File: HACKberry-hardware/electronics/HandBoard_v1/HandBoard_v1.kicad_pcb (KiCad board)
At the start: 2 copper layers, 60.8 x 54.8 mm, 12 parts, among them CON1 BARREL_JACK_MJ179PH, SW1:MAX1 SW_PUSH_SKRGAQD010, SW2:MIN1 SW_PUSH_SKRGAQD010, SW3:Thumb1 SW_PUSH_SKRGAQD010, SW4:Middle1 SW_PUSH_SKRGAQD010, SW5 SWITCH_SS-12SDP2, U1 3-CONDUCTOR_MINIATUIRE_JACK_M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, U2 Arduino_Micro, U3 Seed_Studio_Adjustable_DC/DC_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, U4 Servo_Motor_S03N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

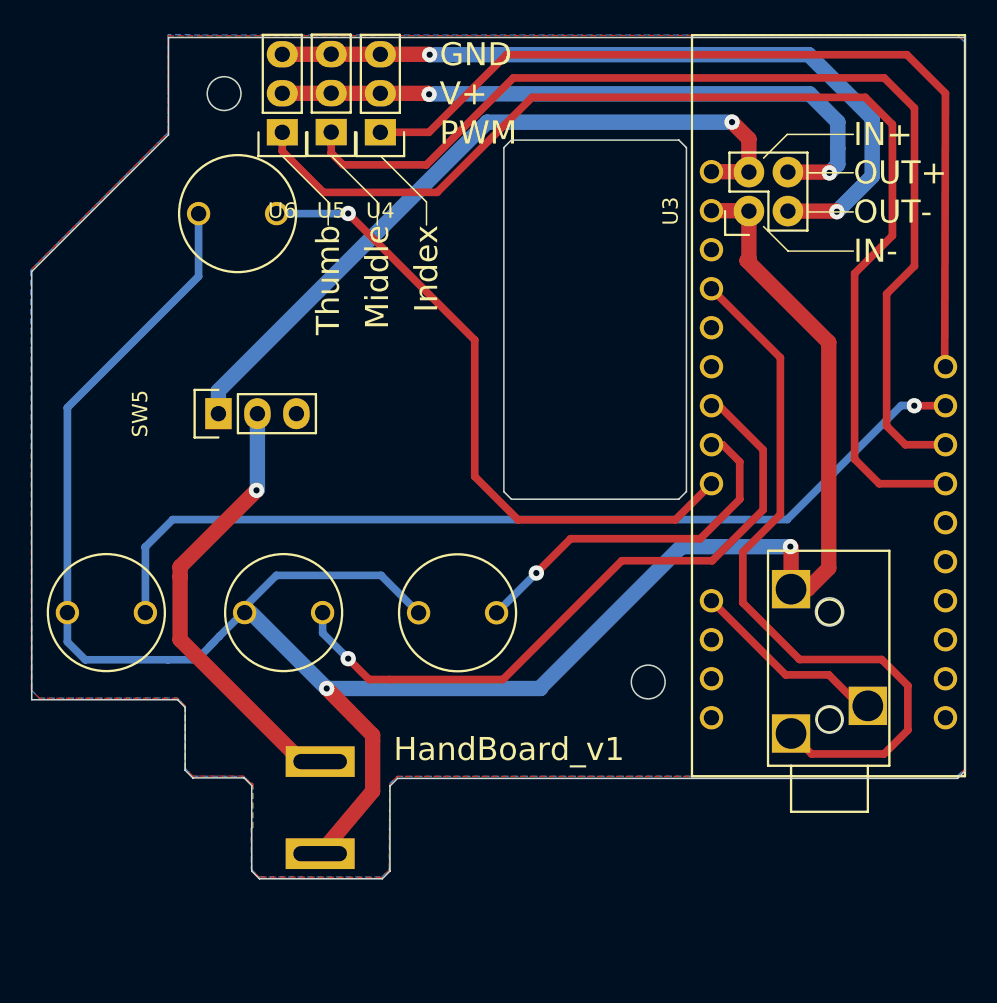
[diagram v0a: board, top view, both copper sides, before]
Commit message: add poly switch to protect servo motor
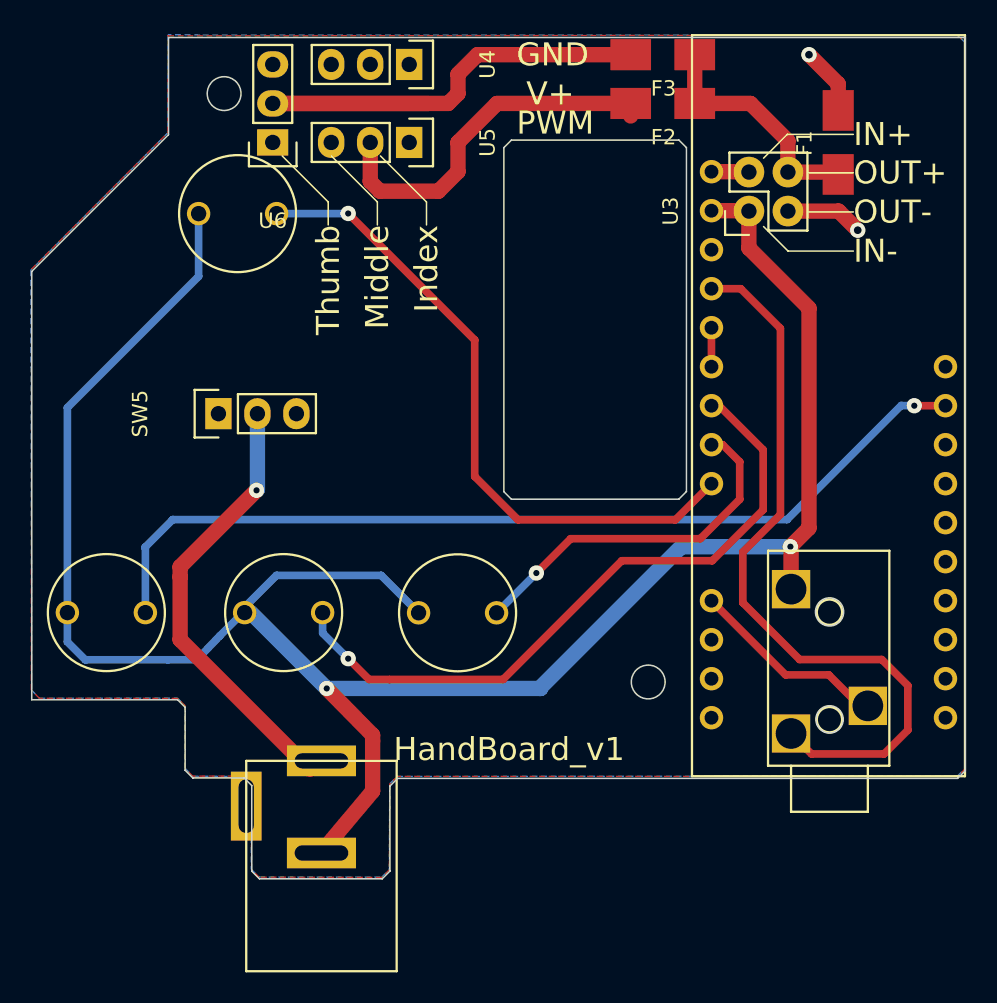
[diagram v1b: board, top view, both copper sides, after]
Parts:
- added F1: FUSE_Hackberry_large, Fuse_Holders_and_Fuses:Fuse_SMD1206_HandSoldering, F.Cu at (149.1, 87.9)
- added F2: FUSE_Hackberry, Fuse_Holders_and_Fuses:Fuse_SMD1206_HandSoldering, F.Cu at (137.7, 85.3)
- added F3: FUSE_Hackberry, Fuse_Holders_and_Fuses:Fuse_SMD1206_HandSoldering, F.Cu at (137.7, 82.1)
- CON1: value BARREL_JACK_MJ179PH -> BARREL_JACK
- U1: value 3-CONDUCTOR_MINIATUIRE_JACK_MJ-4535-3 -> 3-CONDUCTOR_MINIATUIRE_JACK_MJ-4535-3-RESCUE-HandBoard_v1
- U5, U6: value Servo_Motor_MG90S -> Servo_Motor_ES08MD
- moved U5 5.12 mm to (121.2, 87.9), turned to 270 degrees
- moved U4 4.80 mm to (121.2, 82.8), turned to 270 degrees
- moved U6 0.91 mm to (112.3, 87.9)
- moved CON1 0.10 mm to (115.5, 141.8)
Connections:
- SW1:MAX1 pad 1: Net-(CON1-Pad3) -> Net-(CON1-Pad2)
- SW2:MIN1 pad 1: Net-(CON1-Pad3) -> Net-(CON1-Pad2)
- SW3:Thumb1 pad 1: Net-(CON1-Pad3) -> Net-(CON1-Pad2)
- SW4:Middle1 pad 1: Net-(CON1-Pad3) -> Net-(CON1-Pad2)
- U1 pad 1: Net-(CON1-Pad3) -> Net-(CON1-Pad2)
- U2 pad 5V: Net-(U2-Pad5V) -> Net-(U1-Pad2)
- U2 pad GND: Net-(U2-PadGND) -> Net-(CON1-Pad2)
- U3 pad 2: Net-(CON1-Pad3) -> Net-(CON1-Pad2)
- U3 pad 4: Net-(U3-Pad4) -> Net-(F1-Pad1)
- U4 pad 2: Net-(U3-Pad4) -> Net-(F1-Pad2)
- U5 pad 2: Net-(U3-Pad4) -> Net-(F2-Pad2)
- U6 pad 2: Net-(U3-Pad4) -> Net-(F3-Pad2)
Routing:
- net Net-(CON1-Pad3): track 144.4 -> 0.00 mm, vias 2 -> 0
- net Net-(CON1-Pad2): track 0.00 -> 142.3 mm, vias 0 -> 2
- net Net-(U3-Pad4): track 43.2 -> 0.00 mm, vias 2 -> 0
- net Net-(F1-Pad2): track 0.00 -> 36.5 mm, vias 0 -> 1
- net Net-(F3-Pad2): track 0.00 -> 35.5 mm
- net Net-(F2-Pad2): track 0.00 -> 24.1 mm
- net Net-(F1-Pad1): track 0.00 -> 16.3 mm
- net Net-(U3-Pad3): track 50.4 -> 62.3 mm, vias 2 -> 1
- net Net-(U2-Pad5): track 68.6 -> 58.1 mm
- net Net-(U1-Pad2): track 41.7 -> 49.1 mm
- net Net-(U2-Pad5V): track 6.36 -> 0.00 mm
- net Net-(U2-Pad3): track 57.9 -> 52.4 mm
- net Net-(SW5-Pad1): track 48.4 -> 53.3 mm, vias 1 -> 0
- net Net-(U2-Pad6): track 74.8 -> 70.1 mm
- net Net-(U2-PadNC): track 0.00 -> 2.54 mm
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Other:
- copper layers 2 -> 4

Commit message: modified texts and add polygon on internal layers
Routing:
- added copper zone on In1.Cu, net Net-(CON1-Pad3)
- added copper zone on In2.Cu, net Net-(CON1-Pad3)
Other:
- board text removed: "GND"
- board text removed: "PWM"
- board text removed: "V+"
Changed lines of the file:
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@@
     (links 30)
     (no_connects 0)
-    (area 96.561099 80.973599 157.461101 135.863601)
+    (area 95.268 66.530187 157.666101 152.344648)
     (thickness 1.6)
-    (drawings 57)
+    (drawings 50)
     (tracks 182)
     (zones 0)
@@
       (net 17 "Net-(U2-Pad12)"))
   )
+  (gr_text Middle (at 125.0061 91.0336) (layer F.SilkS)
+    (effects (font (size 1.5 1.5) (thickness 0.3)) (justify right))
+  )
   (gr_circle (center 148.5711 125.4336) (end 149.1211 126.1336) (layer Edge.Cuts) (width 0.1))
   (gr_circle (center 148.5711 118.4336) (end 149.3711 118.8836) (layer Edge.Cuts) (width 0.1))
@@
   )
   (gr_text IN- (at 150.1211 94.9336) (layer F.SilkS)
-    (effects (font (size 1.5 1.5) (thickness 0.3)) (justify left))
-  )
-  (gr_text PWM (at 128.1811 86.5886) (layer F.SilkS)
-    (effects (font (size 1.5 1.5) (thickness 0.3)) (justify left))
-  )
-  (gr_text V+ (at 128.8161 84.6836) (layer F.SilkS)
-    (effects (font (size 1.5 1.5) (thickness 0.3)) (justify left))
-  )
-  (gr_text GND (at 128.1811 82.1436) (layer F.SilkS)
     (effects (font (size 1.5 1.5) (thickness 0.3)) (justify left))
   )
@@
   (gr_line (start 147.1211 92.3836) (end 150.1211 92.3836) (angle 90) (layer F.SilkS) (width 0.1))
   (gr_line (start 147.1211 89.8336) (end 150.1211 89.8336) (angle 90) (layer F.SilkS) (width 0.1))
-  (gr_text Index (at 122.3211 93.2336 90) (layer F.SilkS)
-    (effects (font (size 1.5 1.5) (thickness 0.3)) (justify right))
-  )
-  (gr_text Middle (at 119.1211 93.2336 90) (layer F.SilkS)
+  (gr_text Index (at 128.8161 82.7786) (layer F.SilkS)
     (effects (font (size 1.5 1.5) (thickness 0.3)) (justify right))
   )
@@
     (effects (font (size 1.5 1.5) (thickness 0.3)) (justify right))
   )
-  (gr_line (start 122.3211 91.7336) (end 122.3211 93.2336) (angle 90) (layer F.SilkS) (width 0.1))
-  (gr_line (start 119.1211 91.7336) (end 119.1211 93.2336) (angle 90) (layer F.SilkS) (width 0.1))
-  (gr_line (start 119.3211 88.7336) (end 122.3211 91.7336) (angle 90) (layer F.SilkS) (width 0.1))
-  (gr_line (start 116.1211 88.7336) (end 119.1211 91.7336) (angle 90) (layer F.SilkS) (width 0.1))
   (gr_line (start 115.9211 91.7336) (end 115.9211 93.2336) (angle 90) (layer F.SilkS) (width 0.1))
   (gr_line (start 112.9211 88.7336) (end 115.9211 91.7336) (angle 90) (layer F.SilkS) (width 0.1))
@@
       )
     )
+  )
+  (zone (net 1) (net_name "Net-(CON1-Pad3)") (layer In1.Cu) (hatch edge 0.508)
+    (connect_pads (clearance 0.508))
+    (min_thickness 0.254)
+    (fill yes (arc_segments 16) (thermal_gap 0.508) (thermal_bridge_width 0.508))
+    (polygon
+      (pts
+        (xy 157.3911 129.1336) (xy 120.5611 129.1336) (xy 119.9261 129.7686) (xy 119.9261 135.4836) (xy 119.2911 136.1186)
+        (xy 111.6711 136.1186) (xy 111.0361 135.4836) (xy 111.0361 129.7686) (xy 110.4011 129.1336) (xy 107.2261 129.1336)
+        (xy 106.5911 128.4986) (xy 106.5911 124.6886) (xy 105.9561 124.0536) (xy 96.4311 124.0536) (xy 96.4311 96.1136)
+        (xy 105.3211 87.2236) (xy 105.3211 80.8736) (xy 157.3911 80.8736) (xy 157.3911 129.1336)
+      )
+    )
+  )
+  (zone (net 1) (net_name "Net-(CON1-Pad3)") (layer In2.Cu) (hatch edge 0.508)
+    (connect_pads (clearance 0.508))
+    (min_thickness 0.254)
+    (fill yes (arc_segments 16) (thermal_gap 0.508) (thermal_bridge_width 0.508))
+    (polygon
+      (pts
+        (xy 157.3911 129.1336) (xy 120.5611 129.1336) (xy 119.9261 129.7686) (xy 119.9261 135.4836) (xy 119.2911 136.1186)
+        (xy 111.6711 136.1186) (xy 111.0361 135.4836) (xy 111.0361 129.7686) (xy 110.4011 129.1336) (xy 107.2261 129.1336)
+        (xy 106.5911 128.4986) (xy 106.5911 124.6886) (xy 105.9561 124.0536) (xy 96.4311 124.0536) (xy 96.4311 96.1136)
+        (xy 105.3211 87.2236) (xy 105.3211 80.8736) (xy 157.3911 80.8736) (xy 157.3911 129.1336)
+      )
+    )
